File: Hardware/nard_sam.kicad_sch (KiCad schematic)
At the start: 27 parts, among them J1 SIM_Card, J2 SIM_Card, J3 Conn_01x08, J4 Conn_01x10, J5 Conn_01x04, J6 M20-7910842R, J7 M20-7911042R, U1 SEC1210

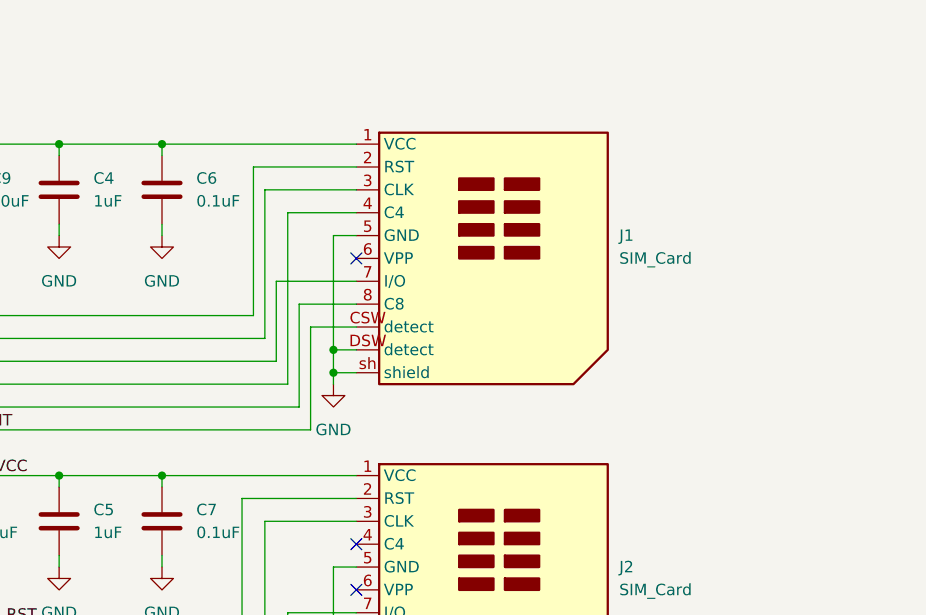
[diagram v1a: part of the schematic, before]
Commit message: added footprint for placing a eSIM chip directly on the PCB
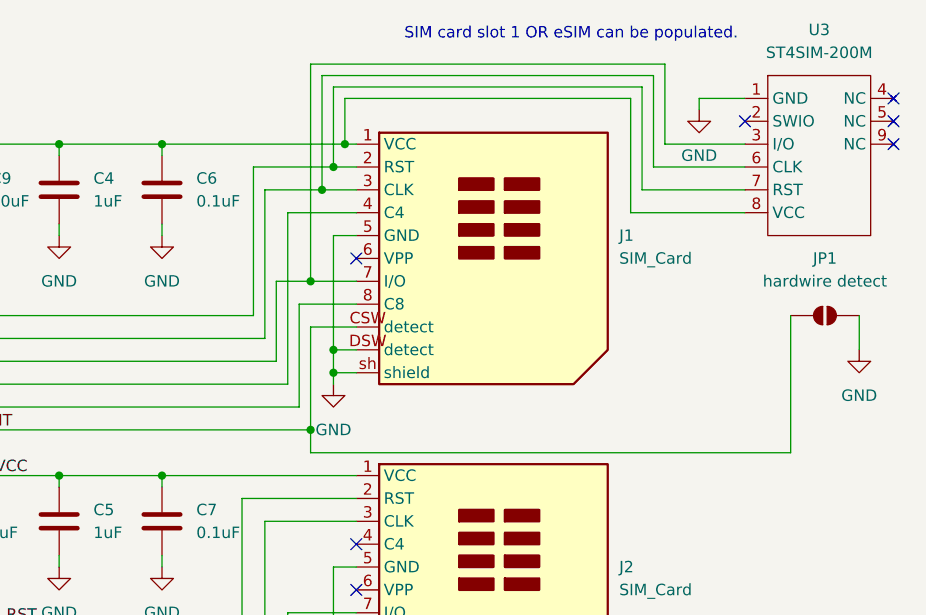
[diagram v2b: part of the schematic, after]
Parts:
- added JP1: hardwire detect, Jumper:SolderJumper-2_P1.3mm_Open_RoundedPad1.0x1.5mm, symbol Jumper:SolderJumper_2_Open
- added U3: ST4SIM-200M, nard_sam:ST4SIM-200M, symbol nard_sam:ST4SIM-200M
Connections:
- net GND: now also JP1.1 (A), U3.1 (GND)
- net SC1_CLK: now also U3.6 (CLK)
- net SC1_IO: now also U3.3 (I/O)
- net SC1_PRSNT: now also JP1.2 (B)
- net SC1_RST: now also U3.7 (RST)
- net SC1_VCC: now also U3.8 (VCC)
- no-connect marks 8 -> 12
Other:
- note added: "SIM card slot 1 OR eSIM can be populated."
